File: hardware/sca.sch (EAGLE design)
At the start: 31 parts

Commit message: lots of layout changes
updated teensy footprint to get rid of internal pins and pads
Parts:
- removed R12, R13, R14, R15: 10k, adafruit:R-US_0204/2V
- removed R19: (no value), adafruit:R-US_0204/2V
- removed U$1: TEENSY_3.5/3.6, Teensy356:TEENSY_3.5/3.6
- added R10, R6, R7, R8, R9: 1M, resistor:R-US_0309/10
- added U$9: TEENSY_3.6_DIL, Teensy_3_and_LC_Series_Boards_v1.4:TEENSY_3.6_DIL
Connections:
- removed net N$1: U$1.0/RX, XB1.DOUT
- removed net N$14: R5.1, U$1.30
- removed net N$15: PH3.2, R14.2, U$1.16/A2
- removed net N$16: R4.1, U$1.29
- removed net N$17: R3.1, U$1.28
- removed net N$18: R1.1, R2.1, U$1.2
- removed net N$19: PH4.2, R15.2, U$1.17/A3
- removed net N$2: PH2.2, R13.2, U$1.15/A1
- removed net N$4: U$1.1/TX, XB1.DIN/!CONFIG
- removed net N$6: PH1.2, R12.2, U$1.14/A0
- removed net N$9: R19.1, R20.2, U$1.A10
- removed net RX: JP4.4, U$1.10/CS
- removed net SCK/SCL: JP2.4, JP7.5, U$1.19/A5/SCL
- removed net SDI/SDA: JP2.6, JP7.4, U$1.18/A4/SDA
- removed net TX: JP4.5, U$1.9/CS
- new net BATT_T: R10.2, R20.2, U$9.3/CAN0-TX/SCL2/PWM
- new net GPS_RX: JP4.4, U$9.10/TX2/PWM
- new net GPS_TX: JP4.5, U$9.9/RX2/PWM
- new net LED_1: R3.1, U$9.28
- new net LED_2: R4.1, U$9.29/T/PWM
- new net LED_3: R5.1, U$9.30/T/PWM
- new net MCU_2: R1.1, R2.1, U$9.2/PWM
- new net MCU_RX: U$9.0/RX1/MOSI1/T, XB1.DOUT
- new net MCU_TX: U$9.1/TX1/MISO1/T, XB1.DIN/!CONFIG
- new net PR_1: PH1.2, R7.2, U$9.14/A0/PWM
- new net PR_2: PH2.2, R6.1, U$9.15/A1/T
- new net PR_3: PH3.2, R8.1, U$9.16/A2/T/PWM
- new net PR_4: PH4.2, R9.1, U$9.17/A3/T/PWM
- new net SCL: JP2.4, JP7.5, U$9.37/A18/SCL1/PWM
- new net SDA: JP2.6, JP7.4, U$9.38/A19/SDA1/PWM
- net +3V3: now also U$9.VIN; no longer U$1.VIN
- net GND: now also R10.1, R6.2, R7.1, R8.2, R9.2, U$9.GND; no longer R12.1, R13.1, R14.1, R15.1, R19.2, U$1.GND

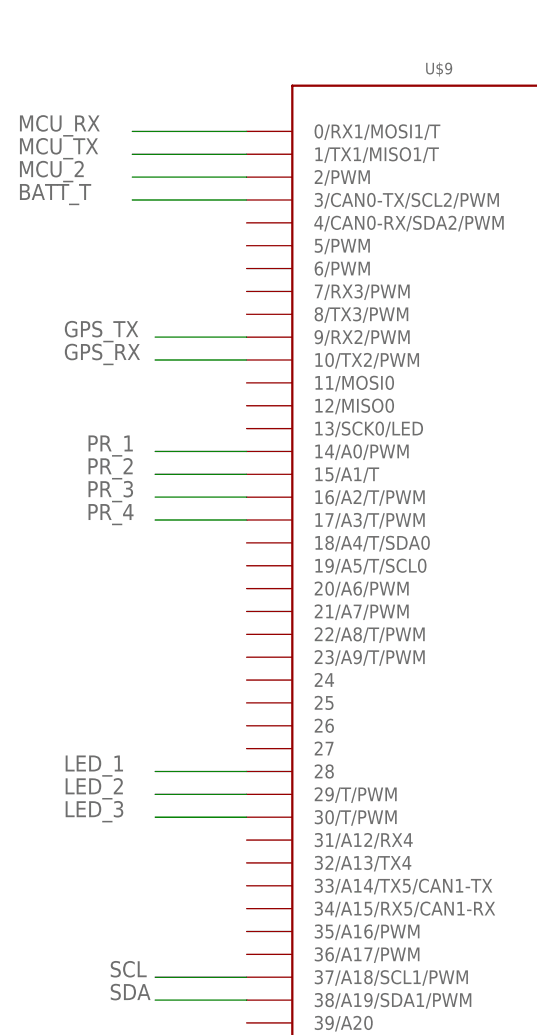
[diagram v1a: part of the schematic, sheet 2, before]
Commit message: initial routing / changed xbee tx/rx for routing reasons
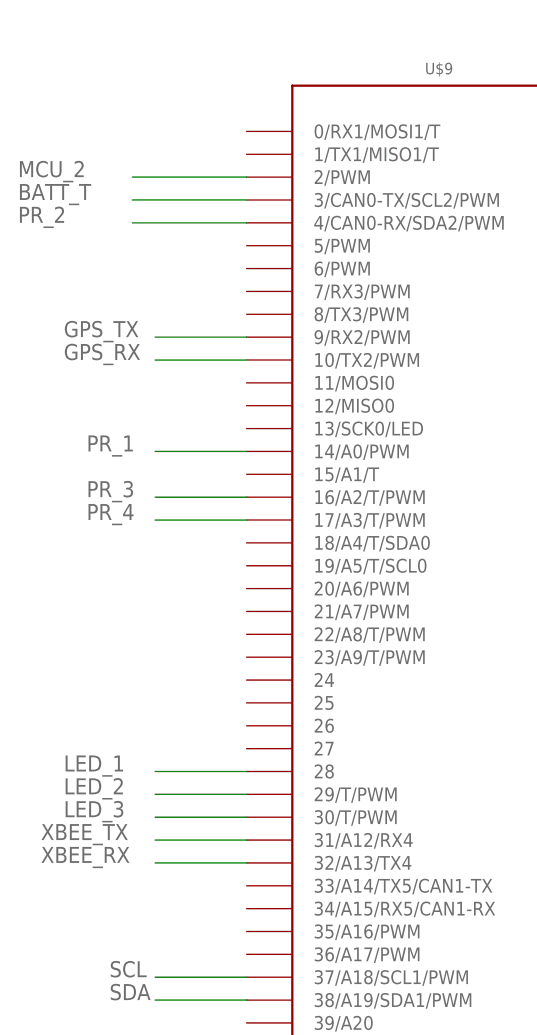
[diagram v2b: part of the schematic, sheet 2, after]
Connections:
- removed net MCU_RX: U$9.0/RX1/MOSI1/T, XB1.DOUT
- removed net MCU_TX: U$9.1/TX1/MISO1/T, XB1.DIN/!CONFIG
- new net XBEE_RX: U$9.32/A13/TX4, XB1.DIN/!CONFIG
- new net XBEE_TX: U$9.31/A12/RX4, XB1.DOUT
- net PR_2: now also U$9.4/CAN0-RX/SDA2/PWM; no longer U$9.15/A1/T
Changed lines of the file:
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@@
 <part name="PH4" library="photo-elements" library_urn="urn:adsk.eagle:library:323" deviceset="A10" device="" package3d_urn="urn:adsk.eagle:package:22201/1" technology="50_09"/>
 <part name="U$33" library="microbuilder" deviceset="GND" device=""/>
-<part name="+3V1" library="supply1" deviceset="+3V3" device=""/>
 <part name="+3V4" library="supply1" deviceset="+3V3" device=""/>
 <part name="R20" library="varistor" library_urn="urn:adsk.eagle:library:410" deviceset="THERMISTOR" device="-2,5" package3d_urn="urn:adsk.eagle:package:30592/1"/>
@@
 <attribute name="VALUE" x="234.696" y="43.18" size="1.27" layer="96"/>
 </instance>
-<instance part="+3V1" gate="G$1" x="135.89" y="127" smashed="yes">
-<attribute name="VALUE" x="133.35" y="121.92" size="1.778" layer="96" rot="R90"/>
-</instance>
 <instance part="+3V4" gate="G$1" x="52.07" y="78.74" smashed="yes" grouprefs="XBEE">
 <attribute name="VALUE" x="54.61" y="81.28" size="1.778" layer="96" rot="R180"/>
@@
 </segment>
 </net>
-<net name="MCU_TX" class="0">
+<net name="XBEE_RX" class="0">
 <segment>
 <pinref part="XB1" gate="G$1" pin="DIN/!CONFIG"/>
@@
 <wire x1="232.41" y1="146.05" x2="232.41" y2="149.86" width="0.1524" layer="91" grouprefs="3V3_REGULATOR"/>
 <junction x="232.41" y="146.05" grouprefs="3V3_REGULATOR"/>
-</segment>
-<segment>
-<wire x1="121.92" y1="119.38" x2="135.89" y2="119.38" width="0.1524" layer="91"/>
-<pinref part="+3V1" gate="G$1" pin="+3V3"/>
-<wire x1="135.89" y1="119.38" x2="135.89" y2="124.46" width="0.1524" layer="91"/>
 </segment>
 <segment>
@@
 </segment>
 </net>
-<net name="MCU_RX" class="0">
+<net name="XBEE_TX" class="0">
 <segment>
 <pinref part="XB1" gate="G$1" pin="DOUT"/>
@@
 </segment>
 </net>
-<net name="MCU_RX" class="0">
-<segment>
-<pinref part="U$9" gate="G$1" pin="0/RX1/MOSI1/T"/>
-<wire x1="55.88" y1="119.38" x2="43.18" y2="119.38" width="0.1524" layer="91"/>
-<label x="30.48" y="119.38" size="1.778" layer="95"/>
-</segment>
-</net>
-<net name="MCU_TX" class="0">
-<segment>
-<pinref part="U$9" gate="G$1" pin="1/TX1/MISO1/T"/>
-<wire x1="55.88" y1="116.84" x2="43.18" y2="116.84" width="0.1524" layer="91"/>
-<label x="30.48" y="116.84" size="1.778" layer="95"/>
-</segment>
-</net>
 <net name="MCU_2" class="0">
 <segment>
@@
 <net name="PR_2" class="0">
 <segment>
-<pinref part="U$9" gate="G$1" pin="15/A1/T"/>
-<wire x1="55.88" y1="81.28" x2="45.72" y2="81.28" width="0.1524" layer="91"/>
-<label x="38.1" y="81.28" size="1.778" layer="95"/>
+<pinref part="U$9" gate="G$1" pin="4/CAN0-RX/SDA2/PWM"/>
+<wire x1="55.88" y1="109.22" x2="43.18" y2="109.22" width="0.1524" layer="91"/>
+<label x="30.48" y="109.22" size="1.778" layer="95"/>
 </segment>
 </net>
@@
 </segment>
 </net>
+<net name="XBEE_TX" class="0">
+<segment>
+<pinref part="U$9" gate="G$1" pin="31/A12/RX4"/>
+<wire x1="55.88" y1="40.64" x2="45.72" y2="40.64" width="0.1524" layer="91"/>
+<label x="33.02" y="40.64" size="1.778" layer="95"/>
+</segment>
+</net>
+<net name="XBEE_RX" class="0">
+<segment>
+<pinref part="U$9" gate="G$1" pin="32/A13/TX4"/>
+<wire x1="55.88" y1="38.1" x2="45.72" y2="38.1" width="0.1524" layer="91"/>
+<label x="33.02" y="38.1" size="1.778" layer="95"/>
+</segment>
+</net>

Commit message: routing...
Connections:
- net PR_4: now also U$9.0/RX1/MOSI1/T; no longer U$9.17/A3/T/PWM
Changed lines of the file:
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@@
 <part name="PH4" library="photo-elements" library_urn="urn:adsk.eagle:library:323" deviceset="A10" device="" package3d_urn="urn:adsk.eagle:package:22201/1" technology="50_09"/>
 <part name="U$33" library="microbuilder" deviceset="GND" device=""/>
+<part name="+3V1" library="supply1" deviceset="+3V3" device=""/>
 <part name="+3V4" library="supply1" deviceset="+3V3" device=""/>
 <part name="R20" library="varistor" library_urn="urn:adsk.eagle:library:410" deviceset="THERMISTOR" device="-2,5" package3d_urn="urn:adsk.eagle:package:30592/1"/>
@@
 <attribute name="VALUE" x="234.696" y="43.18" size="1.27" layer="96"/>
 </instance>
+<instance part="+3V1" gate="G$1" x="135.89" y="127" smashed="yes">
+<attribute name="VALUE" x="133.35" y="121.92" size="1.778" layer="96" rot="R90"/>
+</instance>
 <instance part="+3V4" gate="G$1" x="52.07" y="78.74" smashed="yes" grouprefs="XBEE">
 <attribute name="VALUE" x="54.61" y="81.28" size="1.778" layer="96" rot="R180"/>
@@
 </segment>
 <segment>
+<wire x1="121.92" y1="119.38" x2="135.89" y2="119.38" width="0.1524" layer="91"/>
+<pinref part="+3V1" gate="G$1" pin="+3V3"/>
+<wire x1="135.89" y1="119.38" x2="135.89" y2="124.46" width="0.1524" layer="91"/>
+</segment>
+<segment>
 <pinref part="XB1" gate="G$1" pin="VCC"/>
 <wire x1="43.18" y1="76.2" x2="52.07" y2="76.2" width="0.1524" layer="91" grouprefs="XBEE"/>
@@
 <net name="PR_4" class="0">
 <segment>
-<pinref part="U$9" gate="G$1" pin="17/A3/T/PWM"/>
-<wire x1="55.88" y1="76.2" x2="45.72" y2="76.2" width="0.1524" layer="91"/>
-<label x="38.1" y="76.2" size="1.778" layer="95"/>
-</segment>
-</net>
+<pinref part="U$9" gate="G$1" pin="0/RX1/MOSI1/T"/>
+<wire x1="55.88" y1="119.38" x2="43.18" y2="119.38" width="0.1524" layer="91"/>
+<label x="30.48" y="119.38" size="1.778" layer="95"/>
+</segment>
+</net>
